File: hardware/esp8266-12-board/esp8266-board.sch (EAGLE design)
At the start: 17 parts, among them T1 AMS1117, T2 LM7805

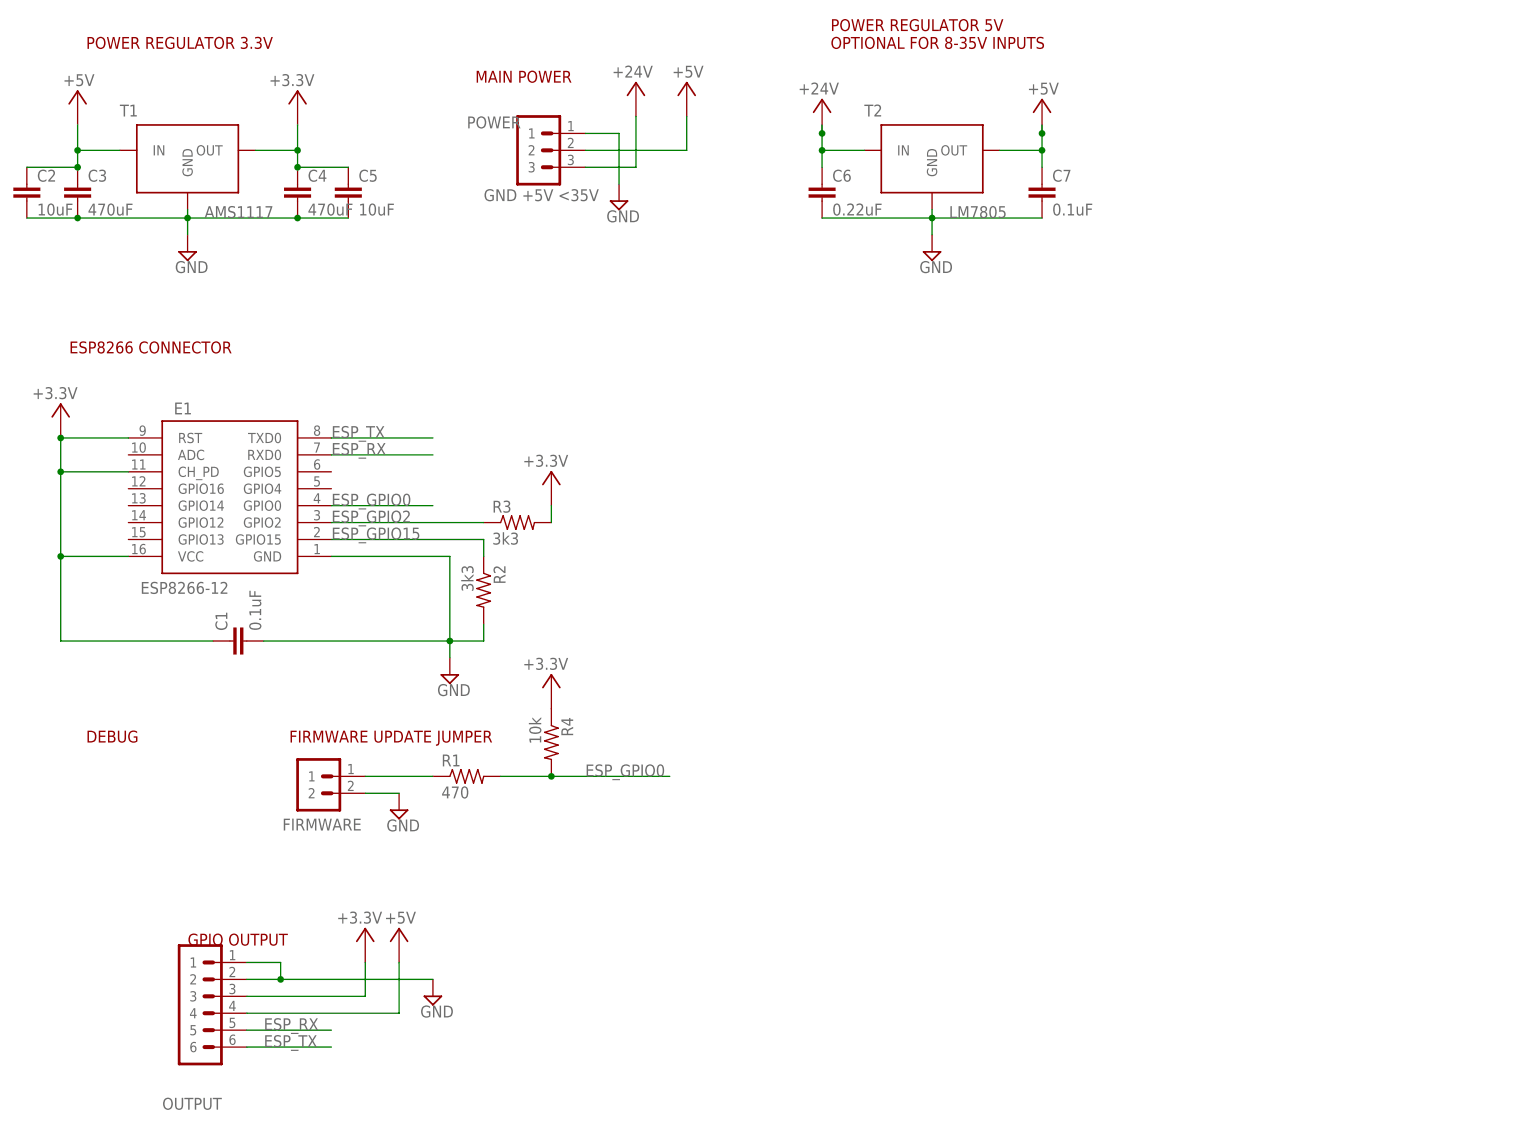
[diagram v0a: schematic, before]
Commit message: Watchdog and SD card addition to ESP12E
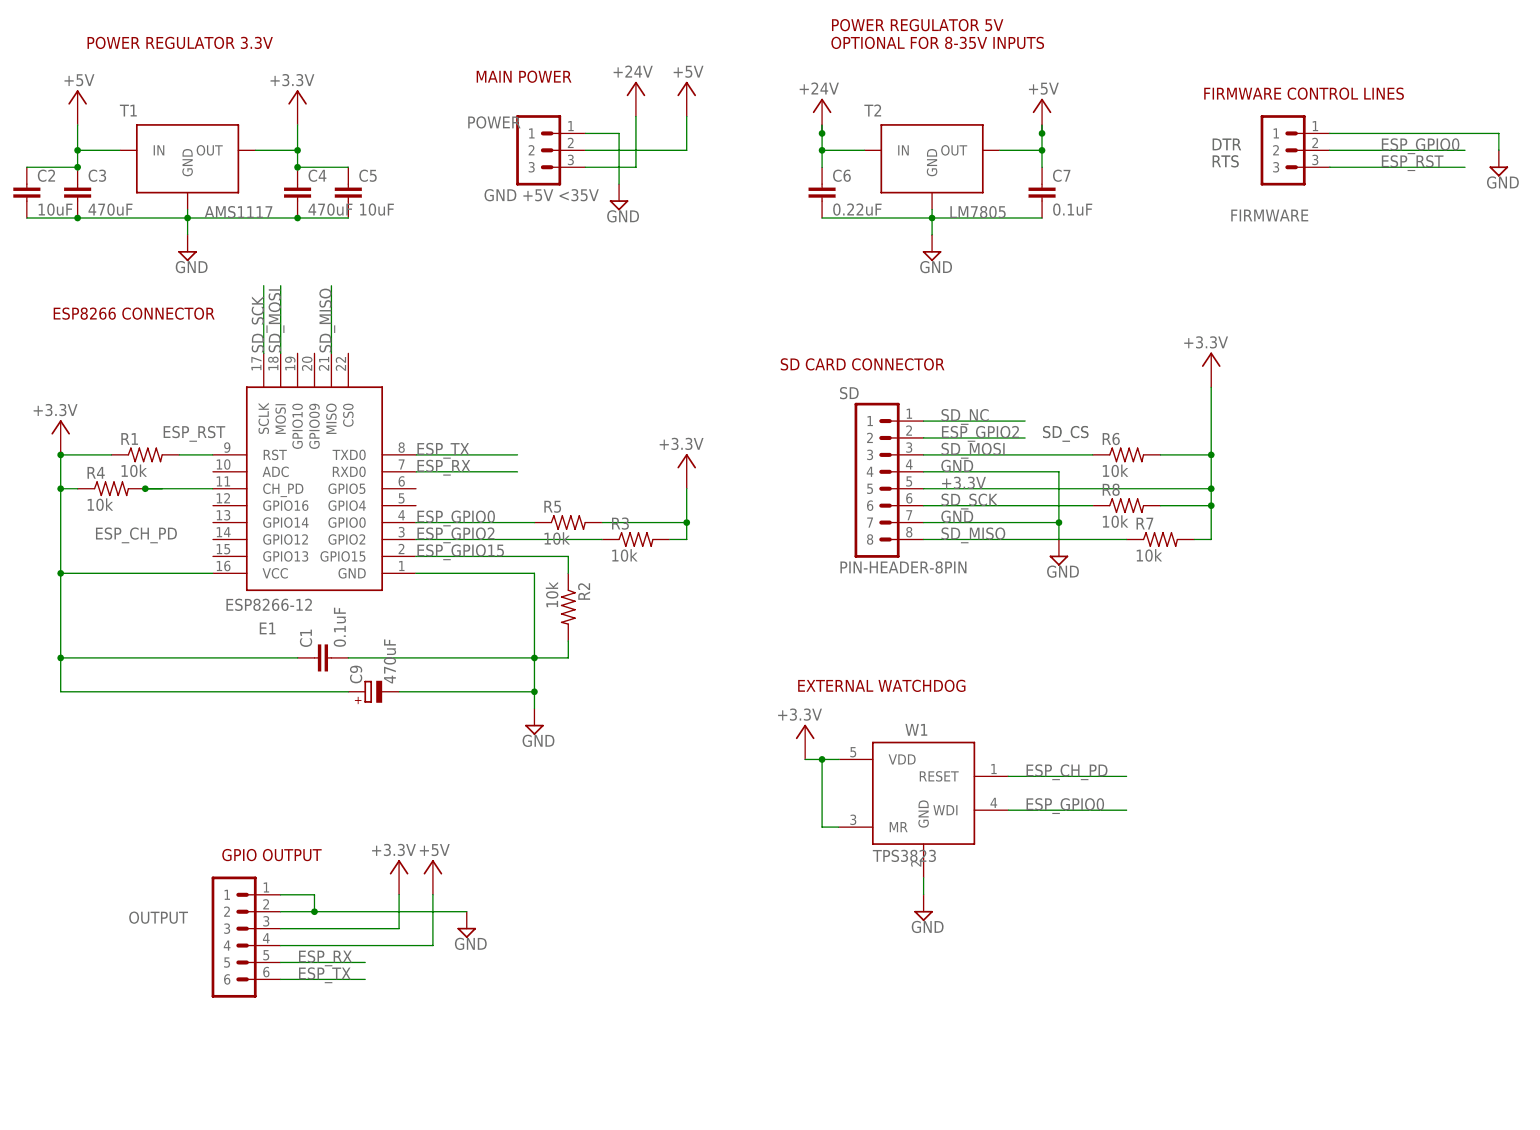
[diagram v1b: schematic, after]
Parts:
- added C9: 470uF, rcl:CPOL-EUE2.5-6
- added R5, R6, R7, R8: 10k, stutz-eagle:RESISTORV1
- added SD: PIN-HEADER-8PIN, stutz-eagle:PIN-HEADER-8PIN
- added W1: TPS3823, stutz-eagle:TPS382X
- FIRMWARE: device stutz-eagle:PIN-HEADER-2PIN -> stutz-eagle:PIN-HEADER-3PIN
- R1: value 470 -> 10k
- R2, R3: value 3k3 -> 10k
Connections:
- removed net N$1: FIRMWARE.1, R1.1
- new net ESP_CH_PD: E1.CH_PD, R4.2, W1.RESET
- new net ESP_RST: E1.RST, FIRMWARE.3, R1.2
- new net SD_MISO: E1.MISO, R7.1, SD.8
- new net SD_MOSI: E1.MOSI, R6.1, SD.3
- new net SD_NC: SD.1
- new net SD_SCK: E1.SCLK, R8.1, SD.6
- net +3.3V: now also C9.+, R1.1, R5.2, R6.2, R7.2, R8.2, SD.5, W1.MR, W1.VDD; no longer E1.CH_PD, E1.RST
- net ESP_GPIO0: now also FIRMWARE.2, R5.1, W1.WDI; no longer R1.2, R4.2
- net ESP_GPIO2: now also SD.2
- net GND: now also C9.-, FIRMWARE.1, SD.4, SD.7, W1.GND; no longer FIRMWARE.2
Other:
- note added: "DTR"
- note added: "EXTERNAL WATCHDOG"
- note added: "FIRMWARE CONTROL LINES"
- note added: "RTS"
- note added: "SD CARD CONNECTOR"
- note added: "SD_CS"
- note removed: "DEBUG"
- note removed: "FIRMWARE UPDATE JUMPER"
- moved on the sheet: C1, OUTPUT, R1, R2, R3, R4

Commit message: commit
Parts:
- removed SD: PIN-HEADER-8PIN, stutz-eagle:PIN-HEADER-8PIN
- added SD1: CS SI GND 3.3V SCK GND SO, stutz-eagle:PIN-HEADER-7PIN
- FIRMWARE: value FIRMWARE -> GND DTR RTS
- OUTPUT: value GND GND 3.3V 5V RX TX -> GND GND 3.3V 5V RX TX
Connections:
- removed net SD_NC: SD.1
- net +3.3V: now also SD1.4; no longer SD.5
- net ESP_GPIO2: now also SD1.1; no longer SD.2
- net GND: now also SD1.3, SD1.6; no longer SD.4, SD.7
- net SD_MISO: now also SD1.7; no longer SD.8
- net SD_MOSI: now also SD1.2; no longer SD.3
- net SD_SCK: now also SD1.5; no longer SD.6
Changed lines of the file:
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@@
 <class number="3" name="power-2A" width="1.143" drill="0">
+</class>
+<class number="4" name="power-1.7A" width="0.8" drill="0">
 </class>
 </classes>
@@
 <part name="SUPPLY1" library="stutz-eagle" deviceset="+5V" device=""/>
 <part name="SUPPLY2" library="supply2" deviceset="GND" device=""/>
-<part name="FIRMWARE" library="stutz-eagle" deviceset="PIN-HEADER-3PIN" device="" value="FIRMWARE"/>
+<part name="FIRMWARE" library="stutz-eagle" deviceset="PIN-HEADER-3PIN" device="" value="GND DTR RTS"/>
 <part name="SUPPLY7" library="supply2" deviceset="GND" device=""/>
-<part name="OUTPUT" library="stutz-eagle" deviceset="PIN-HEADER-6PIN" device="" value="GND GND 3.3V 5V RX TX"/>
+<part name="OUTPUT" library="stutz-eagle" deviceset="PIN-HEADER-6PIN" device="" value="GND GND 3.3V 5V  RX  TX"/>
 <part name="SUPPLY8" library="supply2" deviceset="GND" device=""/>
 <part name="SUPPLY9" library="stutz-eagle" deviceset="+5V" device=""/>
@@
 <part name="R4" library="stutz-eagle" deviceset="RESISTOR" device="V1" value="10k"/>
 <part name="C9" library="rcl" deviceset="CPOL-EU" device="E2.5-6" value="470uF"/>
-<part name="SD" library="stutz-eagle" deviceset="PIN-HEADER-8PIN" device=""/>
 <part name="SUPPLY4" library="supply2" deviceset="GND" device=""/>
 <part name="SUPPLY6" library="stutz-eagle" deviceset="+3.3V" device=""/>
@@
 <part name="SUPPLY11" library="stutz-eagle" deviceset="+3.3V" device=""/>
 <part name="SUPPLY15" library="supply2" deviceset="GND" device=""/>
+<part name="SD1" library="stutz-eagle" deviceset="PIN-HEADER-7PIN" device="" value="CS  SI GND 3.3V SCK GND SO"/>
 </parts>
 <sheets>
@@
 <instance part="R4" gate="G$1" x="20.32" y="99.06"/>
 <instance part="C9" gate="G$1" x="58.42" y="68.58" rot="R90"/>
-<instance part="SD" gate="G$1" x="137.16" y="101.6"/>
-<instance part="SUPPLY4" gate="GND" x="162.56" y="88.9"/>
+<instance part="SUPPLY4" gate="GND" x="162.56" y="86.36"/>
 <instance part="SUPPLY6" gate="G$1" x="185.42" y="116.84"/>
 <instance part="R6" gate="G$1" x="172.72" y="104.14"/>
@@
 <instance part="SUPPLY11" gate="G$1" x="124.46" y="60.96"/>
 <instance part="SUPPLY15" gate="GND" x="142.24" y="35.56"/>
+<instance part="SD1" gate="G$1" x="137.16" y="99.06"/>
 </instances>
 <busses>
 </busses>
 <nets>
-<net name="GND" class="3">
+<net name="GND" class="4">
 <segment>
 <pinref part="T1" gate="G$1" pin="GND"/>
@@
 </segment>
 <segment>
-<pinref part="SD" gate="G$1" pin="4"/>
 <wire x1="142.24" y1="101.6" x2="162.56" y2="101.6" width="0.1524" layer="91"/>
 <label x="144.78" y="101.6" size="1.778" layer="95"/>
 <pinref part="SUPPLY4" gate="GND" pin="GND"/>
 <wire x1="162.56" y1="101.6" x2="162.56" y2="93.98" width="0.1524" layer="91"/>
-<pinref part="SD" gate="G$1" pin="7"/>
-<wire x1="162.56" y1="93.98" x2="162.56" y2="91.44" width="0.1524" layer="91"/>
+<wire x1="162.56" y1="93.98" x2="162.56" y2="88.9" width="0.1524" layer="91"/>
 <wire x1="142.24" y1="93.98" x2="162.56" y2="93.98" width="0.1524" layer="91"/>
 <label x="144.78" y="93.98" size="1.778" layer="95"/>
 <junction x="162.56" y="93.98"/>
+<pinref part="SD1" gate="G$1" pin="6"/>
+<pinref part="SD1" gate="G$1" pin="3"/>
 </segment>
 <segment>
@@
 </segment>
 </net>
-<net name="+3.3V" class="3">
+<net name="+3.3V" class="4">
 <segment>
 <pinref part="SUPPLY16" gate="G$1" pin="+3.3V"/>
@@
 </segment>
 <segment>
-<pinref part="SD" gate="G$1" pin="5"/>
 <label x="144.78" y="99.06" size="1.778" layer="95"/>
 <pinref part="SUPPLY6" gate="G$1" pin="+3.3V"/>
@@
 <junction x="185.42" y="99.06"/>
 <junction x="185.42" y="96.52"/>
+<pinref part="SD1" gate="G$1" pin="4"/>
 </segment>
 <segment>
@@
 </segment>
 </net>
-<net name="+5V" class="3">
+<net name="+5V" class="4">
 <segment>
 <wire x1="15.24" y1="153.67" x2="15.24" y2="149.86" width="0.1524" layer="91"/>
@@
 </segment>
 <segment>
-<pinref part="SD" gate="G$1" pin="2"/>
+<label x="144.78" y="106.68" size="1.778" layer="95"/>
+<pinref part="SD1" gate="G$1" pin="1"/>
 <wire x1="142.24" y1="106.68" x2="157.48" y2="106.68" width="0.1524" layer="91"/>
-<label x="144.78" y="106.68" size="1.778" layer="95"/>
 </segment>
 </net>
@@
 </segment>
 </net>
-<net name="+24V" class="3">
+<net name="+24V" class="4">
 <segment>
 <wire x1="127" y1="153.67" x2="127" y2="152.4" width="0.1524" layer="91"/>
@@
 <net name="SD_MOSI" class="0">
 <segment>
-<pinref part="SD" gate="G$1" pin="3"/>
 <wire x1="142.24" y1="104.14" x2="167.64" y2="104.14" width="0.1524" layer="91"/>
 <label x="144.78" y="104.14" size="1.778" layer="95"/>
 <pinref part="R6" gate="G$1" pin="1"/>
+<pinref part="SD1" gate="G$1" pin="2"/>
 </segment>
 <segment>
@@
 <net name="SD_SCK" class="0">
 <segment>
-<pinref part="SD" gate="G$1" pin="6"/>
 <wire x1="142.24" y1="96.52" x2="167.64" y2="96.52" width="0.1524" layer="91"/>
 <label x="144.78" y="96.52" size="1.778" layer="95"/>
 <pinref part="R8" gate="G$1" pin="1"/>
+<pinref part="SD1" gate="G$1" pin="5"/>
 </segment>
 <segment>
@@
 <net name="SD_MISO" class="0">
 <segment>
-<pinref part="SD" gate="G$1" pin="8"/>
 <label x="144.78" y="91.44" size="1.778" layer="95"/>
 <pinref part="R7" gate="G$1" pin="1"/>
 <wire x1="142.24" y1="91.44" x2="172.72" y2="91.44" width="0.1524" layer="91"/>
+<pinref part="SD1" gate="G$1" pin="7"/>
 </segment>
 <segment>
@@
 </segment>
 </net>
-<net name="SD_NC" class="0">
-<segment>
-<pinref part="SD" gate="G$1" pin="1"/>
-<wire x1="142.24" y1="109.22" x2="157.48" y2="109.22" width="0.1524" layer="91"/>
-<label x="144.78" y="109.22" size="1.778" layer="95"/>
-</segment>
-</net>

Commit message: upload part name
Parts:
- W1: value TPS3823 -> TPS3823-33
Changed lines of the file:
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@@
 <part name="R7" library="stutz-eagle" deviceset="RESISTOR" device="V1" value="10k"/>
 <part name="R8" library="stutz-eagle" deviceset="RESISTOR" device="V1" value="10k"/>
-<part name="W1" library="stutz-eagle" deviceset="TPS382X" device="" value="TPS3823"/>
+<part name="W1" library="stutz-eagle" deviceset="TPS382X" device="" value="TPS3823-33"/>
 <part name="SUPPLY11" library="stutz-eagle" deviceset="+3.3V" device=""/>
 <part name="SUPPLY15" library="supply2" deviceset="GND" device=""/>

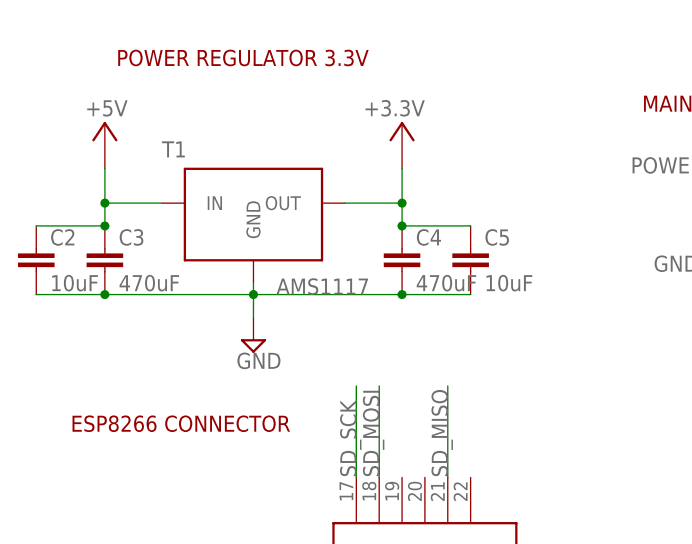
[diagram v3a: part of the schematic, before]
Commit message: updated PCB design during first board assembly
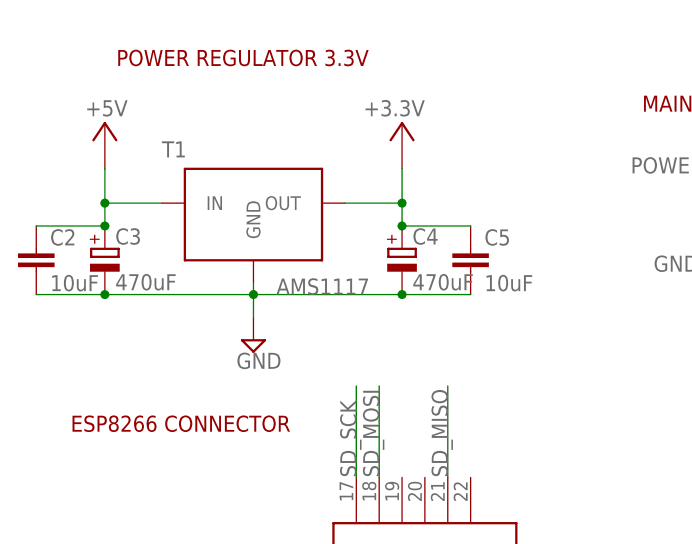
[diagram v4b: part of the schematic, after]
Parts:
- C3: device capacitor-wima:C2.5/2 -> rcl:CPOL-EUE2,5-6E; MPN 1C10Z5U104M050B -> (none)
- C4: device capacitor-wima:C2.5/2 -> rcl:CPOL-EUE2,5-6E
- R1, R2, R3, R4, R5, R6, R7, R8: device stutz-eagle:RESISTORV1 -> stutz-components-library:RESISTORV1
- T2: device stutz-eagle:LM7805 -> stutz-components-library:LM7805
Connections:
- net +3.3V: now also C4.+; no longer C4.1
- net +5V: now also C3.+; no longer C3.1
- net GND: now also C3.-, C4.-; no longer C3.2, C4.2
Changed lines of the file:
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@@
 <?xml version="1.0" encoding="utf-8"?>
 <!DOCTYPE eagle SYSTEM "eagle.dtd">
-<eagle version="7.2.0">
+<eagle version="7.6.0">
 <drawing>
 <settings>
@@
 <part name="SUPPLY16" library="stutz-eagle" deviceset="+3.3V" device=""/>
 <part name="SUPPLY17" library="supply2" deviceset="GND" device=""/>
-<part name="C3" library="capacitor-wima" deviceset="C" device="2.5/2" value="470uF">
-<attribute name="MPN" value="1C10Z5U104M050B"/>
-</part>
-<part name="C4" library="capacitor-wima" deviceset="C" device="2.5/2" value="470uF">
+<part name="C3" library="rcl" deviceset="CPOL-EU" device="E2,5-6E" value="470uF"/>
+<part name="C4" library="rcl" deviceset="CPOL-EU" device="E2,5-6E" value="470uF">
 <attribute name="MPN" value="FK18X5R0J106M"/>
 </part>
@@
 <part name="C5" library="capacitor-wima" deviceset="C" device="2.5/2" value="10uF"/>
 <part name="U$1" library="stutz-eagle" deviceset="+24V" device=""/>
-<part name="T2" library="stutz-eagle" deviceset="LM7805" device="" value="LM7805">
+<part name="T2" library="stutz-components-library" deviceset="LM7805" device="" value="LM7805">
 <attribute name="MPN" value="LM2937ET-3.3"/>
 </part>
@@
 <part name="SUPPLY13" library="supply2" deviceset="GND" device=""/>
 <part name="SUPPLY14" library="stutz-eagle" deviceset="+3.3V" device=""/>
-<part name="R2" library="stutz-eagle" deviceset="RESISTOR" device="V1" value="10k"/>
-<part name="R3" library="stutz-eagle" deviceset="RESISTOR" device="V1" value="10k"/>
+<part name="R2" library="stutz-components-library" deviceset="RESISTOR" device="V1" value="10k"/>
+<part name="R3" library="stutz-components-library" deviceset="RESISTOR" device="V1" value="10k"/>
 <part name="SUPPLY5" library="stutz-eagle" deviceset="+3.3V" device=""/>
-<part name="R5" library="stutz-eagle" deviceset="RESISTOR" device="V1" value="10k"/>
-<part name="R1" library="stutz-eagle" deviceset="RESISTOR" device="V1" value="10k"/>
-<part name="R4" library="stutz-eagle" deviceset="RESISTOR" device="V1" value="10k"/>
+<part name="R5" library="stutz-components-library" deviceset="RESISTOR" device="V1" value="10k"/>
+<part name="R1" library="stutz-components-library" deviceset="RESISTOR" device="V1" value="10k"/>
+<part name="R4" library="stutz-components-library" deviceset="RESISTOR" device="V1" value="10k"/>
 <part name="C9" library="rcl" deviceset="CPOL-EU" device="E2.5-6" value="470uF"/>
 <part name="SUPPLY4" library="supply2" deviceset="GND" device=""/>
 <part name="SUPPLY6" library="stutz-eagle" deviceset="+3.3V" device=""/>
-<part name="R6" library="stutz-eagle" deviceset="RESISTOR" device="V1" value="10k"/>
-<part name="R7" library="stutz-eagle" deviceset="RESISTOR" device="V1" value="10k"/>
-<part name="R8" library="stutz-eagle" deviceset="RESISTOR" device="V1" value="10k"/>
+<part name="R6" library="stutz-components-library" deviceset="RESISTOR" device="V1" value="10k"/>
+<part name="R7" library="stutz-components-library" deviceset="RESISTOR" device="V1" value="10k"/>
+<part name="R8" library="stutz-components-library" deviceset="RESISTOR" device="V1" value="10k"/>
 <part name="W1" library="stutz-eagle" deviceset="TPS382X" device="" value="TPS3823-33"/>
 <part name="SUPPLY11" library="stutz-eagle" deviceset="+3.3V" device=""/>
@@
 <instance part="SUPPLY16" gate="G$1" x="48.26" y="156.21"/>
 <instance part="SUPPLY17" gate="GND" x="31.75" y="134.62"/>
-<instance part="C3" gate="G$1" x="15.24" y="144.78">
-<attribute name="MPN" x="15.24" y="144.78" size="1.778" layer="96" display="off"/>
-</instance>
+<instance part="C3" gate="G$1" x="15.24" y="144.78"/>
 <instance part="C4" gate="G$1" x="48.26" y="144.78">
 <attribute name="MPN" x="48.26" y="144.78" size="1.778" layer="96" display="off"/>
@@
 <wire x1="31.75" y1="139.7" x2="31.75" y2="137.16" width="0.1524" layer="91"/>
 <junction x="31.75" y="139.7"/>
-<pinref part="C3" gate="G$1" pin="2"/>
+<pinref part="C3" gate="G$1" pin="-"/>
 <wire x1="15.24" y1="139.7" x2="31.75" y2="139.7" width="0.1524" layer="91"/>
-<pinref part="C4" gate="G$1" pin="2"/>
+<pinref part="C4" gate="G$1" pin="-"/>
 <wire x1="31.75" y1="139.7" x2="48.26" y2="139.7" width="0.1524" layer="91"/>
 <pinref part="C2" gate="G$1" pin="2"/>
@@
 <segment>
 <pinref part="SUPPLY16" gate="G$1" pin="+3.3V"/>
-<pinref part="C4" gate="G$1" pin="1"/>
+<pinref part="C4" gate="G$1" pin="+"/>
 <wire x1="48.26" y1="153.67" x2="48.26" y2="149.86" width="0.1524" layer="91"/>
 <pinref part="T1" gate="G$1" pin="OUT"/>
@@
 <pinref part="T1" gate="G$1" pin="IN"/>
 <wire x1="15.24" y1="149.86" x2="21.59" y2="149.86" width="0.1524" layer="91"/>
-<pinref part="C3" gate="G$1" pin="1"/>
+<pinref part="C3" gate="G$1" pin="+"/>
 <wire x1="15.24" y1="147.32" x2="15.24" y2="149.86" width="0.1524" layer="91"/>
 <junction x="15.24" y="149.86"/>
